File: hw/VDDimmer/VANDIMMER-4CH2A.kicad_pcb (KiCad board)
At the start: 2 copper layers, 100 x 80 mm, 96 parts, among them J1 USB-C 16P, J10 A2 V+SEL VIN/5V, J11 BTN1, J12 BTN2, J13 EXP 3V3/GND/SDA/SCL/EN/IO0, J14 UART1 3V3/GND/TX/RX, J2 VIN 9-24V, J3 CH1 V+/LED-, J4 CH2 V+/LED-, J5 CH3 V+/LED-, J6 CH4 V+/LED-, J7 ADDR1 V+/D/CLK/GND, J8 ADDR2 V+/D/CLK/GND, J9 A1 V+SEL VIN/5V, Q1 20N06, Q2 20N06, Q3 20N06, Q4 20N06, Q5 SUD50P06-15, U1 ESP32-S3-WROOM-1U-N16, U2 AP63301WU-7, U3 AMS1117-3.3, U4 74HCT125, U5 74HCT125

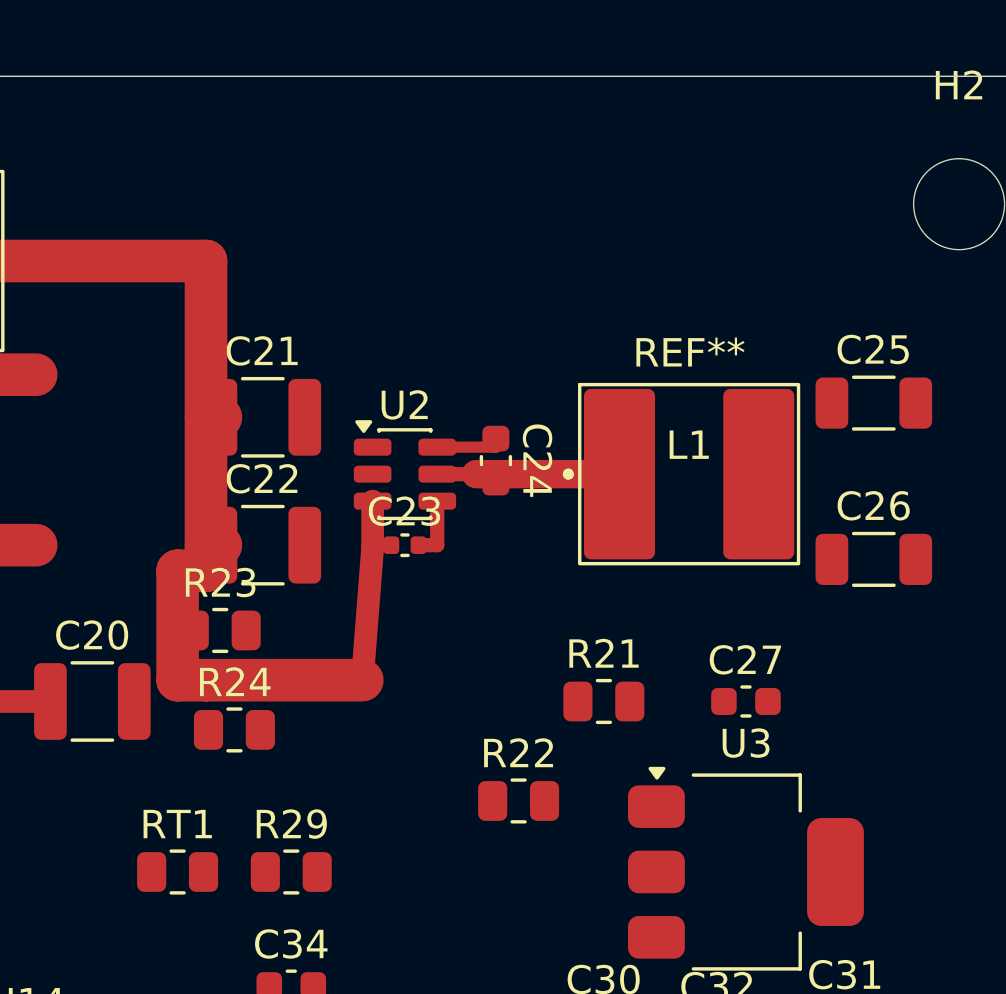
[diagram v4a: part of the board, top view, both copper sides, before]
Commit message: Move FB divider clear of SW/L1; route FB, EN, +5V sense
FB divider (R21/R22/C27) relocated from below-right of the buck -- where the
FB trace would have run under L1 and alongside the switch node -- to the free
strip above U2, on the opposite side of the IC from SW. EN divider (R23/R24)
moved to the same strip so its VIN_BUCK tap comes off the x=169 bus without
crossing the 1.5 mm VIN_BUCK distribution bus at y=81.25.

Measured (F.Cu, saved file):
- FB net copper to nearest SW copper: 1.57 mm (pin-escape, U2 pin1 to pin5
  are 2.27 mm apart on the package -- this is the package floor, not layout)
- FB parallel run alongside SW within 3 mm: 0.00 mm (no x-overlap anywhere)
- FB net copper to nearest L1 pad: 3.86 mm; no FB copper under L1 or SW
- FB trace length U2.1 -> R22.1: 8.6 mm, all on F.Cu
- +5V feedback sense taken at C25.1 (output cap Kelvin point), routed over the
  top at y=62.0: 12.0 mm from the SW trace, 6.1 mm from L1 pad1

DRC 0 errors, 0 phantom pads, unconnected 197 -> 190.

Co-Authored-By: Claude Opus 5 (1M context) <noreply@anthropic.com>
Claude-Session: https://claude.ai/code/session_01XeXr1isxVCg8kRo5Eh8BHM
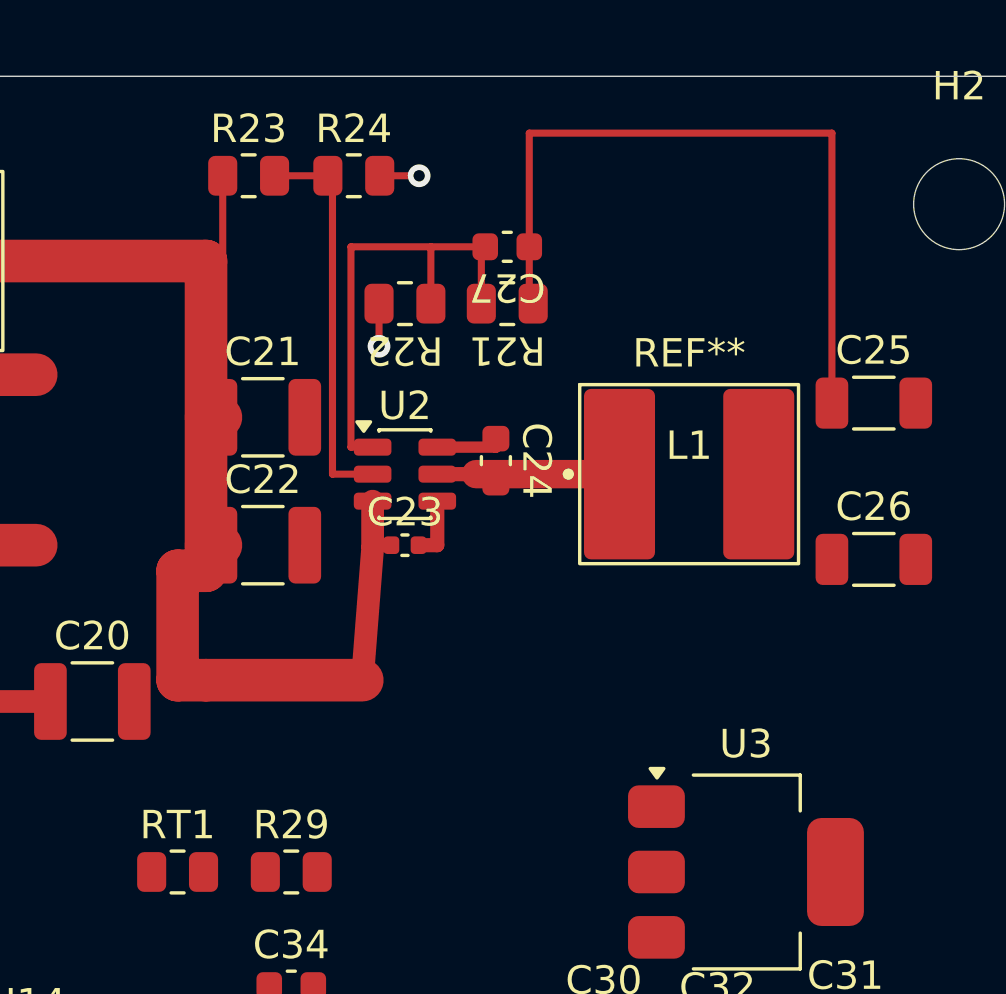
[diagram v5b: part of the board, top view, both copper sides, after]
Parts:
- moved R24 19.9 mm to (174.2, 63.5)
- moved C27 18.1 mm to (179.6, 66.0), turned to 180 degrees
- moved R22 18.0 mm to (176.0, 68.0), turned to 180 degrees
- moved R23 16.0 mm to (170.5, 63.5)
- moved R21 14.4 mm to (179.6, 68.0), turned to 180 degrees
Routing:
- net +5V: track 0.00 -> 26.2 mm
- net /Power/FB: track 0.00 -> 16.5 mm
- net /Power/EN_BUCK: track 0.00 -> 13.8 mm
- net /Power/VIN_BUCK: track 63.8 -> 66.8 mm
- net GND: track 1.96 -> 4.84 mm, vias 0 -> 2
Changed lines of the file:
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@@
 	(footprint "Resistor_SMD:R_0805_2012Metric"
 		(layer "F.Cu")
-		(at 170 83)
+		(at 174.2 63.5)
 		(descr "Resistor SMD 0805 (2012 Metric), square (rectangular) end terminal, IPC-7351 nominal, (Body size source: IPC-SM-782 page 72, https://www.pcb-3d.com/wordpress/wp-content/uploads/ipc-sm-782a_amendment_1_and_2.pdf)")
 		(tags "resistor")
@@
 	(footprint "Resistor_SMD:R_0805_2012Metric"
 		(layer "F.Cu")
-		(at 169.5 79.5)
+		(at 170.5 63.5)
 		(descr "Resistor SMD 0805 (2012 Metric), square (rectangular) end terminal, IPC-7351 nominal, (Body size source: IPC-SM-782 page 72, https://www.pcb-3d.com/wordpress/wp-content/uploads/ipc-sm-782a_amendment_1_and_2.pdf)")
 		(tags "resistor")
@@
 	(footprint "Capacitor_SMD:C_0603_1608Metric"
 		(layer "F.Cu")
-		(at 188 82)
+		(at 179.6 66 180)
 		(descr "Capacitor SMD 0603 (1608 Metric), square (rectangular) end terminal, IPC-7351 nominal, (Body size source: IPC-SM-782 page 76, https://www.pcb-3d.com/wordpress/wp-content/uploads/ipc-sm-782a_amendment_1_and_2.pdf)")
 		(tags "capacitor")
 		(property "Reference" "C27"
-			(at 0 -1.43 0)
+			(at 0 -1.43 180)
 			(unlocked yes)
 			(layer "F.SilkS")
@@
 		)
 		(property "Value" "22pF"
-			(at 0 1.43 0)
+			(at 0 1.43 180)
 			(unlocked yes)
 			(layer "F.SilkS")
@@
 		)
 		(property "Datasheet" ""
-			(at 0 0 0)
+			(at 0 0 180)
 			(layer "F.Fab")
 			(hide yes)
@@
 		)
 		(property "Description" ""
-			(at 0 0 0)
+			(at 0 0 180)
 			(layer "F.Fab")
 			(hide yes)
@@
 		)
 		(property "KiLib_Generator" "SMD_2terminal_chip_molded"
-			(at 0 0 0)
+			(at 0 0 180)
 			(layer "F.SilkS")
 			(hide yes)
@@
 		(duplicate_pad_numbers_are_jumpers no)
 		(fp_line
-			(start -0.14058 -0.51)
-			(end 0.14058 -0.51)
+			(start -0.14058 0.51)
+			(end 0.14058 0.51)
 			(stroke
 				(width 0.12)
@@
 		)
 		(fp_line
-			(start -0.14058 0.51)
-			(end 0.14058 0.51)
+			(start -0.14058 -0.51)
+			(end 0.14058 -0.51)
 			(stroke
 				(width 0.12)
@@
 		)
 		(fp_text user "${REFERENCE}"
-			(at 0 0 0)
+			(at 0 0 180)
 			(unlocked yes)
 			(layer "F.Fab")
@@
 		)
 		(pad "1" smd roundrect
-			(at -0.775 0)
+			(at -0.775 0 180)
 			(size 0.9 0.95)
 			(layers "F.Cu" "F.Mask" "F.Paste")
@@
 		)
 		(pad "2" smd roundrect
-			(at 0.775 0)
+			(at 0.775 0 180)
 			(size 0.9 0.95)
 			(layers "F.Cu" "F.Mask" "F.Paste")
@@
 	(footprint "Resistor_SMD:R_0805_2012Metric"
 		(layer "F.Cu")
-		(at 183 82)
+		(at 179.6 68 180)
 		(descr "Resistor SMD 0805 (2012 Metric), square (rectangular) end terminal, IPC-7351 nominal, (Body size source: IPC-SM-782 page 72, https://www.pcb-3d.com/wordpress/wp-content/uploads/ipc-sm-782a_amendment_1_and_2.pdf)")
 		(tags "resistor")
 		(property "Reference" "R21"
-			(at 0 -1.65 0)
+			(at 0 -1.65 180)
 			(unlocked yes)
 			(layer "F.SilkS")
@@
 		)
 		(property "Value" "52.3k 1%"
-			(at 0 1.65 0)
+			(at 0 1.65 180)
 			(unlocked yes)
 			(layer "F.SilkS")
@@
 		)
 		(property "Datasheet" ""
-			(at 0 0 0)
+			(at 0 0 180)
 			(layer "F.Fab")
 			(hide yes)
@@
 		)
 		(property "Description" ""
-			(at 0 0 0)
+			(at 0 0 180)
 			(layer "F.Fab")
 			(hide yes)
@@
 		)
 		(property "KiLib_Generator" "SMD_2terminal_chip_molded"
-			(at 0 0 0)
+			(at 0 0 180)
 			(layer "F.SilkS")
 			(hide yes)
@@
 		(duplicate_pad_numbers_are_jumpers no)
 		(fp_line
-			(start -0.227064 -0.735)
-			(end 0.227064 -0.735)
+			(start -0.227064 0.735)
+			(end 0.227064 0.735)
 			(stroke
 				(width 0.12)
@@
 		)
 		(fp_line
-			(start -0.227064 0.735)
-			(end 0.227064 0.735)
+			(start -0.227064 -0.735)
+			(end 0.227064 -0.735)
 			(stroke
 				(width 0.12)
@@
 		)
 		(fp_text user "${REFERENCE}"
-			(at 0 0 0)
+			(at 0 0 180)
 			(unlocked yes)
 			(layer "F.Fab")
@@
 		)
 		(pad "1" smd roundrect
-			(at -0.9125 0)
+			(at -0.9125 0 180)
 			(size 1.025 1.4)
 			(layers "F.Cu" "F.Mask" "F.Paste")
@@
 		)
 		(pad "2" smd roundrect
-			(at 0.9125 0)
+			(at 0.9125 0 180)
 			(size 1.025 1.4)
 			(layers "F.Cu" "F.Mask" "F.Paste")
@@
 	(footprint "Resistor_SMD:R_0805_2012Metric"
 		(layer "F.Cu")
-		(at 180 85.5)
+		(at 176 68 180)
 		(descr "Resistor SMD 0805 (2012 Metric), square (rectangular) end terminal, IPC-7351 nominal, (Body size source: IPC-SM-782 page 72, https://www.pcb-3d.com/wordpress/wp-content/uploads/ipc-sm-782a_amendment_1_and_2.pdf)")
 		(tags "resistor")
 		(property "Reference" "R22"
-			(at 0 -1.65 0)
+			(at 0 -1.65 180)
 			(unlocked yes)
 			(layer "F.SilkS")
@@
 		)
 		(property "Value" "10k 1%"
-			(at 0 1.65 0)
+			(at 0 1.65 180)
 			(unlocked yes)
 			(layer "F.SilkS")
@@
 		)
 		(property "Datasheet" ""
-			(at 0 0 0)
+			(at 0 0 180)
 			(layer "F.Fab")
 			(hide yes)
@@
 		)
 		(property "Description" ""
-			(at 0 0 0)
+			(at 0 0 180)
 			(layer "F.Fab")
 			(hide yes)
@@
 		)
 		(property "KiLib_Generator" "SMD_2terminal_chip_molded"
-			(at 0 0 0)
+			(at 0 0 180)
 			(layer "F.SilkS")
 			(hide yes)
@@
 		(duplicate_pad_numbers_are_jumpers no)
 		(fp_line
-			(start -0.227064 -0.735)
-			(end 0.227064 -0.735)
+			(start -0.227064 0.735)
+			(end 0.227064 0.735)
 			(stroke
 				(width 0.12)
@@
 		)
 		(fp_line
-			(start -0.227064 0.735)
-			(end 0.227064 0.735)
+			(start -0.227064 -0.735)
+			(end 0.227064 -0.735)
 			(stroke
 				(width 0.12)
@@
 		)
 		(fp_text user "${REFERENCE}"
-			(at 0 0 0)
+			(at 0 0 180)
 			(unlocked yes)
 			(layer "F.Fab")
@@
 		)
 		(pad "1" smd roundrect
-			(at -0.9125 0)
+			(at -0.9125 0 180)
 			(size 1.025 1.4)
 			(layers "F.Cu" "F.Mask" "F.Paste")
@@
 		)
 		(pad "2" smd roundrect
-			(at 0.9125 0)
+			(at 0.9125 0 180)
 			(size 1.025 1.4)
 			(layers "F.Cu" "F.Mask" "F.Paste")
@@
 	)
 	(segment
+		(start 180.375 62)
+		(end 180.375 68)
+		(width 0.25)
+		(layer "F.Cu")
+		(net "+5V")
+	)
+	(segment
+		(start 191.025 62)
+		(end 180.375 62)
+		(width 0.25)
+		(layer "F.Cu")
+		(net "+5V")
+	)
+	(segment
+		(start 191.025 71.5)
+		(end 191.025 62)
+		(width 0.25)
+		(layer "F.Cu")
+		(net "+5V")
+	)
+	(segment
 		(start 176.48 76.5)
 		(end 177.137 76.5)
@@
 	)
 	(segment
+		(start 175.113 63.5)
+		(end 176.5 63.5)
+		(width 0.25)
+		(layer "F.Cu")
+		(net "GND")
+	)
+	(segment
+		(start 175.088 68)
+		(end 175.088 69.5)
+		(width 0.25)
+		(layer "F.Cu")
+		(net "GND")
+	)
+	(segment
 		(start 177.137 76.5)
 		(end 177.137 75.2)
@@
 		(net "GND")
 	)
+	(via
+		(at 175.088 69.5)
+		(size 0.8)
+		(drill 0.4)
+		(layers "F.Cu" "B.Cu")
+		(net "GND")
+	)
+	(via
+		(at 176.5 63.5)
+		(size 0.8)
+		(drill 0.4)
+		(layers "F.Cu" "B.Cu")
+		(net "GND")
+	)
 	(segment
 		(start 142.96 67.72)
@@
 	)
 	(segment
+		(start 173.45 74)
+		(end 174.863 74)
+		(width 0.25)
+		(layer "F.Cu")
+		(net "/Power/EN_BUCK")
+	)
+	(segment
+		(start 171.412 63.5)
+		(end 173.287 63.5)
+		(width 0.25)
+		(layer "F.Cu")
+		(net "/Power/EN_BUCK")
+	)
+	(segment
+		(start 173.45 63.5)
+		(end 173.45 74)
+		(width 0.25)
+		(layer "F.Cu")
+		(net "/Power/EN_BUCK")
+	)
+	(segment
 		(start 118 69)
 		(end 125.5 69)
@@
 	)
 	(segment
+		(start 169.588 63.5)
+		(end 169.588 66.5)
+		(width 0.25)
+		(layer "F.Cu")
+		(net "/Power/VIN_BUCK")
+	)
+	(segment
 		(start 161 76.5)
 		(end 163.025 76.5)
@@
 	)
 	(segment
+		(start 174.1 66)
+		(end 178.825 66)
+		(width 0.25)
+		(layer "F.Cu")
+		(net "/Power/FB")
+	)
+	(segment
+		(start 174.863 73.05)
+		(end 174.1 73.05)
+		(width 0.25)
+		(layer "F.Cu")
+		(net "/Power/FB")
+	)
+	(segment
+		(start 176.912 66)
+		(end 176.912 68)
+		(width 0.25)
+		(layer "F.Cu")
+		(net "/Power/FB")
+	)
+	(segment
+		(start 178.688 66)
+		(end 178.688 68)
+		(width 0.25)
+		(layer "F.Cu")
+		(net "/Power/FB")
+	)
+	(segment
+		(start 174.1 73.05)
+		(end 174.1 66)
+		(width 0.25)
+		(layer "F.Cu")
+		(net "/Power/FB")
+	)
+	(segment

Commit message: Re-pin U1: move 8 nets off the bottom row onto free right-column GPIOs
Measured blocker: the escape from U1's bottom row past x=149.6 has a free
window of y 110.06..113.38 (3.32 mm) = 6 lanes at 0.25 mm trace / 0.2 mm
clearance, plus 3 more reachable via the D3-D4 slot into the corridor above Q4.
Nine eastbound nets left that row (GATE_IN1-4, ADDR1_DIN, ADDR2_DIN, ADDR_CLK,
I2C_SDA, EN_MCU) and four westbound returned through it (GDRV1-4): 13 needed,
9 available. Not routable on 2 layers with B.Cu reserved for GND.

Reassignment (schematic only, no BOM change, firmware-configurable):
  GATE_IN1  IO4  pad4  -> IO3   pad15   y 108.985
  GATE_IN2  IO5  pad5  -> IO46  pad16   y 107.715
  GATE_IN3  IO6  pad6  -> IO12  pad20   y 102.635
  GATE_IN4  IO7  pad7  -> IO13  pad21   y 101.365
  I2C_SDA   IO8  pad12 -> IO14  pad22   y 100.095  (level with J13.3)
  ADDR1_DIN IO15 pad8  -> IO21  pad23   y  98.825
  ADDR2_DIN IO16 pad9  -> IO47  pad24   y  97.555
  ADDR_CLK  IO17 pad10 -> IO45  pad26   y  95.015

Strapping-pin safety: IO45 (VDD_SPI select) and IO46 (ROM print control) both
drive 74HCT125 inputs only, which are high-Z, so their internal pulldowns hold
them low through reset. IO3 (JTAG source select) likewise sees only a high-Z
74HCT125 input, and its strap only selects JTAG routing. I2C_SDA, which may
carry an off-board pull-up via J13, went to IO14 -- not a strapping pin.

Corner load after: GDRV1-4 west (4) + EN_MCU east (1) = 5 of 6 lanes.
ERC 0/0. DRC 0 errors, 0 phantom pads, unconnected 190.

Co-Authored-By: Claude Opus 5 (1M context) <noreply@anthropic.com>
Claude-Session: https://claude.ai/code/session_01XeXr1isxVCg8kRo5Eh8BHM
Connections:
- U1 pad 10: ADDR_CLK -> unconnected-(U1-IO17-Pad10)
- U1 pad 12: /MCU/I2C_SDA -> unconnected-(U1-IO8-Pad12)
- U1 pad 15: unconnected-(U1-IO3-Pad15) -> GATE_IN1
- U1 pad 16: unconnected-(U1-IO46-Pad16) -> GATE_IN2
- U1 pad 20: unconnected-(U1-IO12-Pad20) -> GATE_IN3
- U1 pad 21: unconnected-(U1-IO13-Pad21) -> GATE_IN4
- U1 pad 22: unconnected-(U1-IO14-Pad22) -> /MCU/I2C_SDA
- U1 pad 23: unconnected-(U1-IO21-Pad23) -> ADDR1_DIN
- U1 pad 24: unconnected-(U1-IO47-Pad24) -> ADDR2_DIN
- U1 pad 26: unconnected-(U1-IO45-Pad26) -> ADDR_CLK
- U1 pad 4: GATE_IN1 -> unconnected-(U1-IO4-Pad4)
- U1 pad 5: GATE_IN2 -> unconnected-(U1-IO5-Pad5)
- U1 pad 6: GATE_IN3 -> unconnected-(U1-IO6-Pad6)
- U1 pad 7: GATE_IN4 -> unconnected-(U1-IO7-Pad7)
- U1 pad 8: ADDR1_DIN -> unconnected-(U1-IO15-Pad8)
- U1 pad 9: ADDR2_DIN -> unconnected-(U1-IO16-Pad9)
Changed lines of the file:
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@@
 			(size 1.5 0.9)
 			(layers "F.Cu" "F.Mask" "F.Paste")
-			(net "GATE_IN1")
+			(net "unconnected-(U1-IO4-Pad4)")
 		)
 		(pad "5" smd rect
@@
 			(size 1.5 0.9)
 			(layers "F.Cu" "F.Mask" "F.Paste")
-			(net "GATE_IN2")
+			(net "unconnected-(U1-IO5-Pad5)")
 		)
 		(pad "6" smd rect
@@
 			(size 1.5 0.9)
 			(layers "F.Cu" "F.Mask" "F.Paste")
-			(net "GATE_IN3")
+			(net "unconnected-(U1-IO6-Pad6)")
 		)
 		(pad "7" smd rect
@@
 			(size 1.5 0.9)
 			(layers "F.Cu" "F.Mask" "F.Paste")
-			(net "GATE_IN4")
+			(net "unconnected-(U1-IO7-Pad7)")
 		)
 		(pad "8" smd rect
@@
 			(size 1.5 0.9)
 			(layers "F.Cu" "F.Mask" "F.Paste")
-			(net "ADDR1_DIN")
+			(net "unconnected-(U1-IO15-Pad8)")
 		)
 		(pad "9" smd rect
@@
 			(size 1.5 0.9)
 			(layers "F.Cu" "F.Mask" "F.Paste")
-			(net "ADDR2_DIN")
+			(net "unconnected-(U1-IO16-Pad9)")
 		)
 		(pad "10" smd rect
@@
 			(size 1.5 0.9)
 			(layers "F.Cu" "F.Mask" "F.Paste")
-			(net "ADDR_CLK")
+			(net "unconnected-(U1-IO17-Pad10)")
 		)
 		(pad "11" smd rect
@@
 			(size 1.5 0.9)
 			(layers "F.Cu" "F.Mask" "F.Paste")
-			(net "/MCU/I2C_SDA")
+			(net "unconnected-(U1-IO8-Pad12)")
 		)
 		(pad "13" smd rect
@@
 			(size 1.5 0.9)
 			(layers "F.Cu" "F.Mask" "F.Paste")
-			(net "unconnected-(U1-IO3-Pad15)")
+			(net "GATE_IN1")
 		)
 		(pad "16" smd rect
@@
 			(size 1.5 0.9)
 			(layers "F.Cu" "F.Mask" "F.Paste")
-			(net "unconnected-(U1-IO46-Pad16)")
+			(net "GATE_IN2")
 		)
 		(pad "17" smd rect
@@
 			(size 1.5 0.9)
 			(layers "F.Cu" "F.Mask" "F.Paste")
-			(net "unconnected-(U1-IO12-Pad20)")
+			(net "GATE_IN3")
 		)
 		(pad "21" smd rect
@@
 			(size 1.5 0.9)
 			(layers "F.Cu" "F.Mask" "F.Paste")
-			(net "unconnected-(U1-IO13-Pad21)")
+			(net "GATE_IN4")
 		)
 		(pad "22" smd rect
@@
 			(size 1.5 0.9)
 			(layers "F.Cu" "F.Mask" "F.Paste")
-			(net "unconnected-(U1-IO14-Pad22)")
+			(net "/MCU/I2C_SDA")
 		)
 		(pad "23" smd rect
@@
 			(size 1.5 0.9)
 			(layers "F.Cu" "F.Mask" "F.Paste")
-			(net "unconnected-(U1-IO21-Pad23)")
+			(net "ADDR1_DIN")
 		)
 		(pad "24" smd rect
@@
 			(size 1.5 0.9)
 			(layers "F.Cu" "F.Mask" "F.Paste")
-			(net "unconnected-(U1-IO47-Pad24)")
+			(net "ADDR2_DIN")
 		)
 		(pad "25" smd rect
@@
 			(size 1.5 0.9)
 			(layers "F.Cu" "F.Mask" "F.Paste")
-			(net "unconnected-(U1-IO45-Pad26)")
+			(net "ADDR_CLK")
 		)
 		(pad "27" smd rect
